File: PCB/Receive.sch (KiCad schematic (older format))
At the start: 40 parts

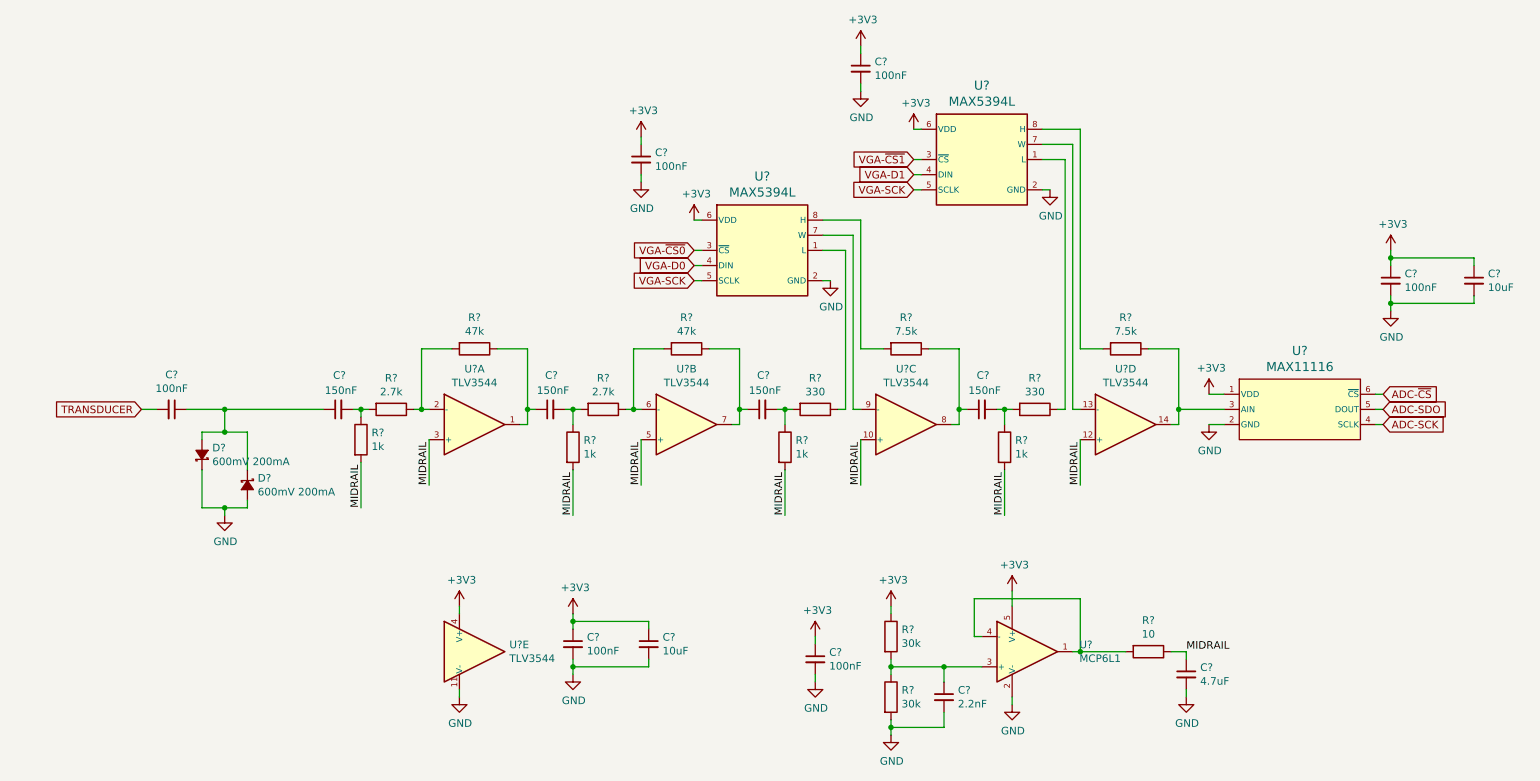
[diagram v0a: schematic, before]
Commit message: Switch 3.3V analog circuitry to low noise supply, fix pin classifications on some parts, swap 9V connector for 10V
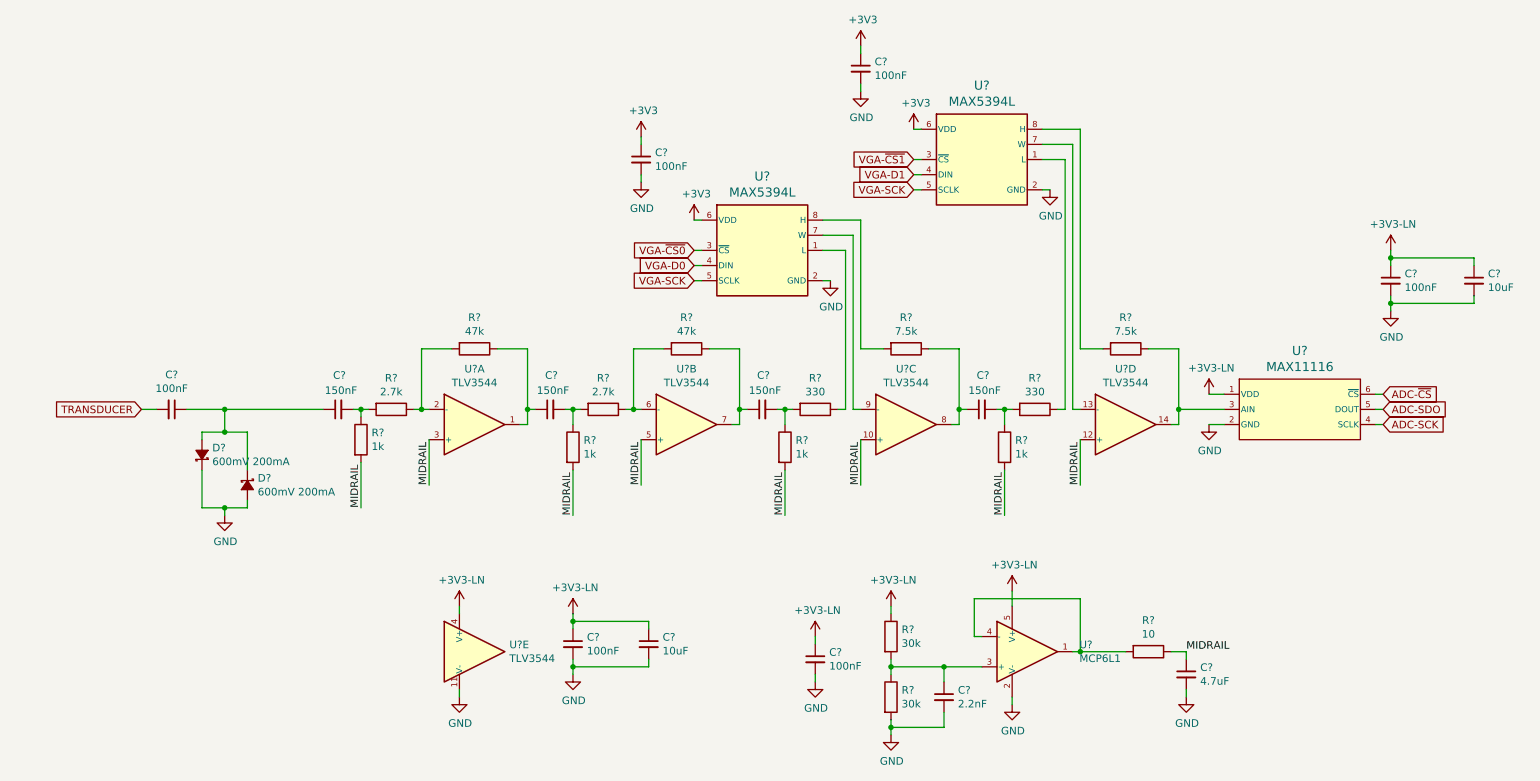
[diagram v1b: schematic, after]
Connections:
- net +3V3: no longer C?.1, C?.1, C?.1, C?.1, C?.1, R?.1, U?.1 (VDD), U?.4 (V+), U?.5 (V+)
- new net +3V3-LN: C?.1, C?.1, C?.1, C?.1, C?.1, R?.1, U?.1 (VDD), U?.4 (V+), U?.5 (V+)
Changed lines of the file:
@@
-$EndComp
-$Comp
-L power:+3V3 #PWR?
-U 1 1 5DE6A184
-P 8650 3650
-F 0 "#PWR?" H 8650 3500 50  0001 C CNN
-F 1 "+3V3" H 8665 3823 50  0000 C CNN
-F 2 "" H 8650 3650 50  0001 C CNN
-F 3 "" H 8650 3650 50  0001 C CNN
-	1    8650 3650
-	1    0    0    -1
 $EndComp
 $Comp
@@
 $EndComp
 $Comp
-L power:+3V3 #PWR?
-U 1 1 5E3D46BE
-P 9850 2700
-F 0 "#PWR?" H 9850 2550 50  0001 C CNN
-F 1 "+3V3" H 9865 2873 50  0000 C CNN
-F 2 "" H 9850 2700 50  0001 C CNN
-F 3 "" H 9850 2700 50  0001 C CNN
-	1    9850 2700
-	1    0    0    -1
-$EndComp
-$Comp
 L power:GND #PWR?
 U 1 1 5E3D4BAC
@@
 	2150 3750 2800 3750
 $Comp
-L power:+3V3 #PWR?
-U 1 1 5DF4FCE8
-P 6050 5250
-F 0 "#PWR?" H 6050 5100 50  0001 C CNN
-F 1 "+3V3" H 6065 5423 50  0000 C CNN
-F 2 "" H 6050 5250 50  0001 C CNN
-F 3 "" H 6050 5250 50  0001 C CNN
-	1    6050 5250
-	1    0    0    -1
-$EndComp
-$Comp
 L power:GND #PWR?
 U 1 1 5DF502DD
@@
 Wire Wire Line
 	4450 5450 4450 5500
-$Comp
-L power:+3V3 #PWR?
-U 1 1 5DF52ADC
-P 4450 5100
-F 0 "#PWR?" H 4450 4950 50  0001 C CNN
-F 1 "+3V3" H 4465 5273 50  0000 C CNN
-F 2 "" H 4450 5100 50  0001 C CNN
-F 3 "" H 4450 5100 50  0001 C CNN
-	1    4450 5100
-	1    0    0    -1
-$EndComp
-$Comp
-L power:+3V3 #PWR?
-U 1 1 5DF58761
-P 3700 5050
-F 0 "#PWR?" H 3700 4900 50  0001 C CNN
-F 1 "+3V3" H 3715 5223 50  0000 C CNN
-F 2 "" H 3700 5050 50  0001 C CNN
-F 3 "" H 3700 5050 50  0001 C CNN
-	1    3700 5050
-	1    0    0    -1
-$EndComp
 $Comp
 L power:GND #PWR?
@@
 Wire Wire Line
 	6100 2900 6150 2900
-$Comp
-L power:+3V3 #PWR?
-U 1 1 5DFD98EC
-P 5250 2500
-F 0 "#PWR?" H 5250 2350 50  0001 C CNN
-F 1 "+3V3" H 5265 2673 50  0000 C CNN
-F 2 "" H 5250 2500 50  0001 C CNN
-F 3 "" H 5250 2500 50  0001 C CNN
-	1    5250 2500
-	1    0    0    -1
-$EndComp
 Wire Wire Line
 	5250 2500 5300 2500
@@
 Wire Wire Line
 	7550 2300 7600 2300
-$Comp
-L power:+3V3 #PWR?
-U 1 1 5E033FD3
-P 6700 1900
-F 0 "#PWR?" H 6700 1750 50  0001 C CNN
-F 1 "+3V3" H 6715 2073 50  0000 C CNN
-F 2 "" H 6700 1900 50  0001 C CNN
-F 3 "" H 6700 1900 50  0001 C CNN
-	1    6700 1900
-	1    0    0    -1
-$EndComp
 Wire Wire Line
 	6700 1900 6750 1900
-$Comp
-L power:+3V3 #PWR?
-U 1 1 5E052B0A
-P 7350 4950
-F 0 "#PWR?" H 7350 4800 50  0001 C CNN
-F 1 "+3V3" H 7365 5123 50  0000 C CNN
-F 2 "" H 7350 4950 50  0001 C CNN
-F 3 "" H 7350 4950 50  0001 C CNN
-	1    7350 4950
-	1    0    0    -1
-$EndComp
 Wire Wire Line
 	7350 4950 7350 5050
@@
 Wire Wire Line
 	7300 4450 7300 4150
-$Comp
-L power:+3V3 #PWR?
-U 1 1 5E0A28B9
-P 6550 5050
-F 0 "#PWR?" H 6550 4900 50  0001 C CNN
-F 1 "+3V3" H 6565 5223 50  0000 C CNN
-F 2 "" H 6550 5050 50  0001 C CNN
-F 3 "" H 6550 5050 50  0001 C CNN
-	1    6550 5050
-	1    0    0    -1
-$EndComp
 $Comp
 L Device:R R?
@@
 	6350 2500 6350 3350
 $Comp
-L power:+3V3 #PWR?
-U 1 1 5E150771
-P 4900 1950
-F 0 "#PWR?" H 4900 1800 50  0001 C CNN
-F 1 "+3V3" H 4915 2123 50  0000 C CNN
-F 2 "" H 4900 1950 50  0001 C CNN
-F 3 "" H 4900 1950 50  0001 C CNN
-	1    4900 1950
-	1    0    0    -1
-$EndComp
-$Comp
 L power:GND #PWR?
 U 1 1 5E15077B
@@
 Wire Wire Line
 	4900 1950 4900 2000
-$Comp
-L power:+3V3 #PWR?
-U 1 1 5E168AD7
-P 6350 1350
-F 0 "#PWR?" H 6350 1200 50  0001 C CNN
-F 1 "+3V3" H 6365 1523 50  0000 C CNN
-F 2 "" H 6350 1350 50  0001 C CNN
-F 3 "" H 6350 1350 50  0001 C CNN
-	1    6350 1350
-	1    0    0    -1
-$EndComp
 $Comp
 L power:GND #PWR?
@@
 Wire Wire Line
 	5250 2900 5300 2900
+$Comp
+L power:+3V3 #PWR?
+U 1 1 5E033FD3
+P 6700 1900
+F 0 "#PWR?" H 6700 1750 50  0001 C CNN
+F 1 "+3V3" H 6715 2073 50  0000 C CNN
+F 2 "" H 6700 1900 50  0001 C CNN
+F 3 "" H 6700 1900 50  0001 C CNN
+	1    6700 1900
+	1    0    0    -1
+$EndComp
+$Comp
+L power:+3V3 #PWR?
+U 1 1 5E168AD7
+P 6350 1350
+F 0 "#PWR?" H 6350 1200 50  0001 C CNN
+F 1 "+3V3" H 6365 1523 50  0000 C CNN
+F 2 "" H 6350 1350 50  0001 C CNN
+F 3 "" H 6350 1350 50  0001 C CNN
+	1    6350 1350
+	1    0    0    -1
+$EndComp
+$Comp
+L power:+3V3 #PWR?
+U 1 1 5DFD98EC
+P 5250 2500
+F 0 "#PWR?" H 5250 2350 50  0001 C CNN
+F 1 "+3V3" H 5265 2673 50  0000 C CNN
+F 2 "" H 5250 2500 50  0001 C CNN
+F 3 "" H 5250 2500 50  0001 C CNN
+	1    5250 2500
+	1    0    0    -1
+$EndComp
+$Comp
+L power:+3V3 #PWR?
+U 1 1 5E150771
+P 4900 1950
+F 0 "#PWR?" H 4900 1800 50  0001 C CNN
+F 1 "+3V3" H 4915 2123 50  0000 C CNN
+F 2 "" H 4900 1950 50  0001 C CNN
+F 3 "" H 4900 1950 50  0001 C CNN
+	1    4900 1950
+	1    0    0    -1
+$EndComp
+$Comp
+L Parts:+3V3-LN #PWR?
+U 1 1 5E2A82B0
+P 8650 3650
+F 0 "#PWR?" H 8650 3500 50  0001 C CNN
+F 1 "+3V3-LN" H 8665 3823 50  0000 C CNN
+F 2 "" H 8650 3650 50  0001 C CNN
+F 3 "" H 8650 3650 50  0001 C CNN
+	1    8650 3650
+	1    0    0    -1
+$EndComp
+$Comp
+L Parts:+3V3-LN #PWR?
+U 1 1 5E2AAEEA
+P 6550 5050
+F 0 "#PWR?" H 6550 4900 50  0001 C CNN
+F 1 "+3V3-LN" H 6565 5223 50  0000 C CNN
+F 2 "" H 6550 5050 50  0001 C CNN
+F 3 "" H 6550 5050 50  0001 C CNN
+	1    6550 5050
+	1    0    0    -1
+$EndComp
+$Comp
+L Parts:+3V3-LN #PWR?
+U 1 1 5E2AD2A7
+P 9850 2700
+F 0 "#PWR?" H 9850 2550 50  0001 C CNN
+F 1 "+3V3-LN" H 9865 2873 50  0000 C CNN
+F 2 "" H 9850 2700 50  0001 C CNN
+F 3 "" H 9850 2700 50  0001 C CNN
+	1    9850 2700
+	1    0    0    -1
+$EndComp
+$Comp
+L Parts:+3V3-LN #PWR?
+U 1 1 5E2AFA32
+P 7350 4950
+F 0 "#PWR?" H 7350 4800 50  0001 C CNN
+F 1 "+3V3-LN" H 7365 5123 50  0000 C CNN
+F 2 "" H 7350 4950 50  0001 C CNN
+F 3 "" H 7350 4950 50  0001 C CNN
+	1    7350 4950
+	1    0    0    -1
+$EndComp
+$Comp
+L Parts:+3V3-LN #PWR?
+U 1 1 5E2AFFB8
+P 6050 5250
+F 0 "#PWR?" H 6050 5100 50  0001 C CNN
+F 1 "+3V3-LN" H 6065 5423 50  0000 C CNN
+F 2 "" H 6050 5250 50  0001 C CNN
+F 3 "" H 6050 5250 50  0001 C CNN
+	1    6050 5250
+	1    0    0    -1
+$EndComp
+$Comp
+L Parts:+3V3-LN #PWR?
+U 1 1 5E2B0647
+P 4450 5100
+F 0 "#PWR?" H 4450 4950 50  0001 C CNN
+F 1 "+3V3-LN" H 4465 5273 50  0000 C CNN
+F 2 "" H 4450 5100 50  0001 C CNN
+F 3 "" H 4450 5100 50  0001 C CNN
+	1    4450 5100
+	1    0    0    -1
+$EndComp
+$Comp
+L Parts:+3V3-LN #PWR?
+U 1 1 5E2B0FA3
+P 3700 5050
+F 0 "#PWR?" H 3700 4900 50  0001 C CNN
+F 1 "+3V3-LN" H 3715 5223 50  0000 C CNN
+F 2 "" H 3700 5050 50  0001 C CNN
+F 3 "" H 3700 5050 50  0001 C CNN
+	1    3700 5050
+	1    0    0    -1
+$EndComp
 $EndSCHEMATC

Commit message: Annotate schematic, simplify transmit circuit, shuffle receive opamp stages, reorder buttons so they match net names, reorder connectors to simplify routing, begin arranging parts on PCB
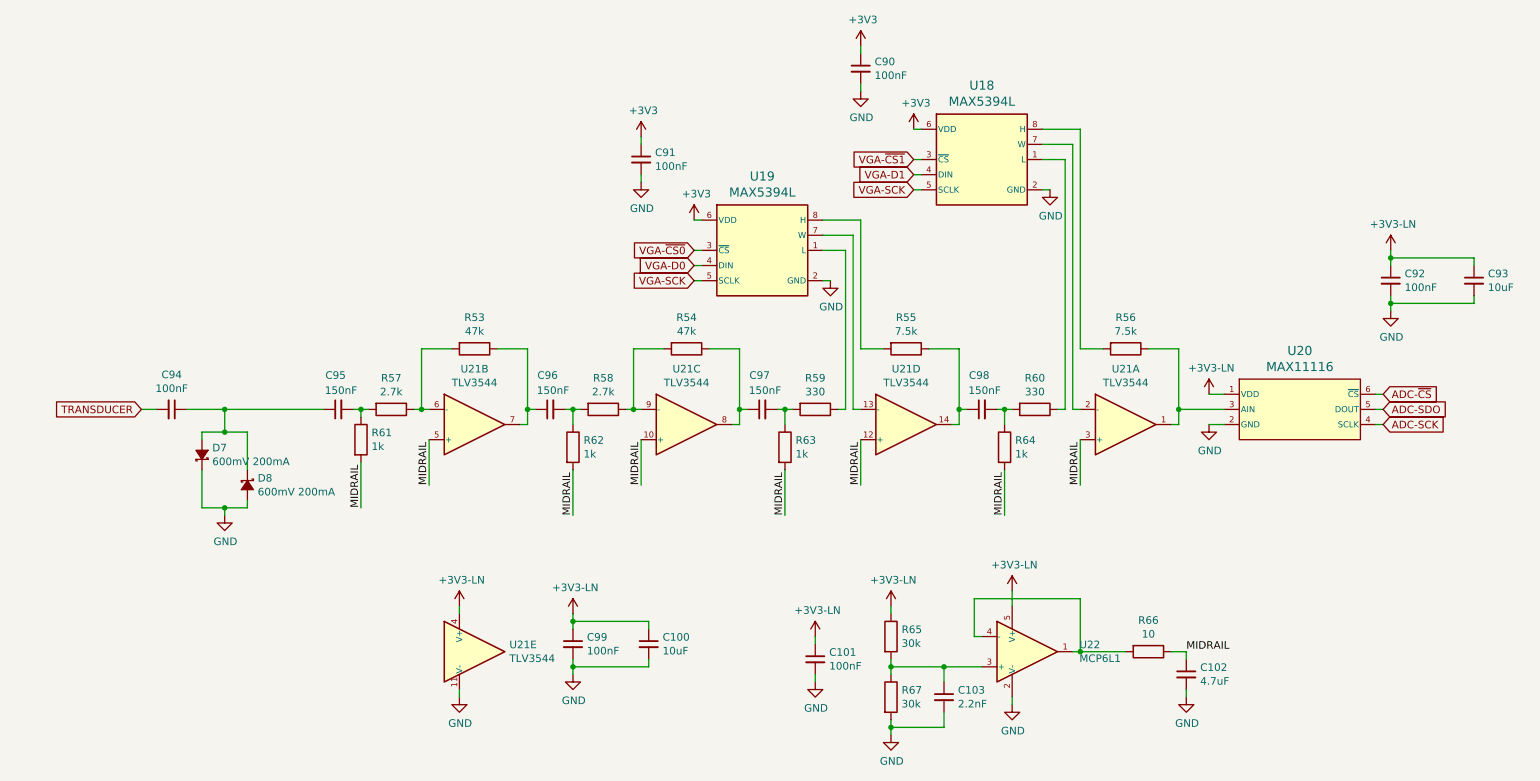
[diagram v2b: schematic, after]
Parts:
- gave numbers to parts that had none: 36
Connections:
- net at R56.1, U20.3 (AIN): now also U21.1; no longer U21.14
- net at C96.1, R53.1: now also U21.7; no longer U21.1
- net at R53.2, R57.1: now also U21.6 (-); no longer U21.2 (-)
- net at R54.2, R58.1: now also U21.9 (-); no longer U21.6 (-)
- net at C97.1, R54.1: now also U21.8; no longer U21.7
- net at C98.1, R55.1: now also U21.14; no longer U21.8
- net at U19.7 (W): now also U21.13 (-); no longer U21.9 (-)
- net at U18.7 (W): now also U21.2 (-); no longer U21.13 (-)
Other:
- moved on the sheet: U21A, U21B, U21C, U21D

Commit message: Begin layout around FPGA and microcontroller, rearrange some connections to FPGA and microcontroller, change groupings of optional debug pins
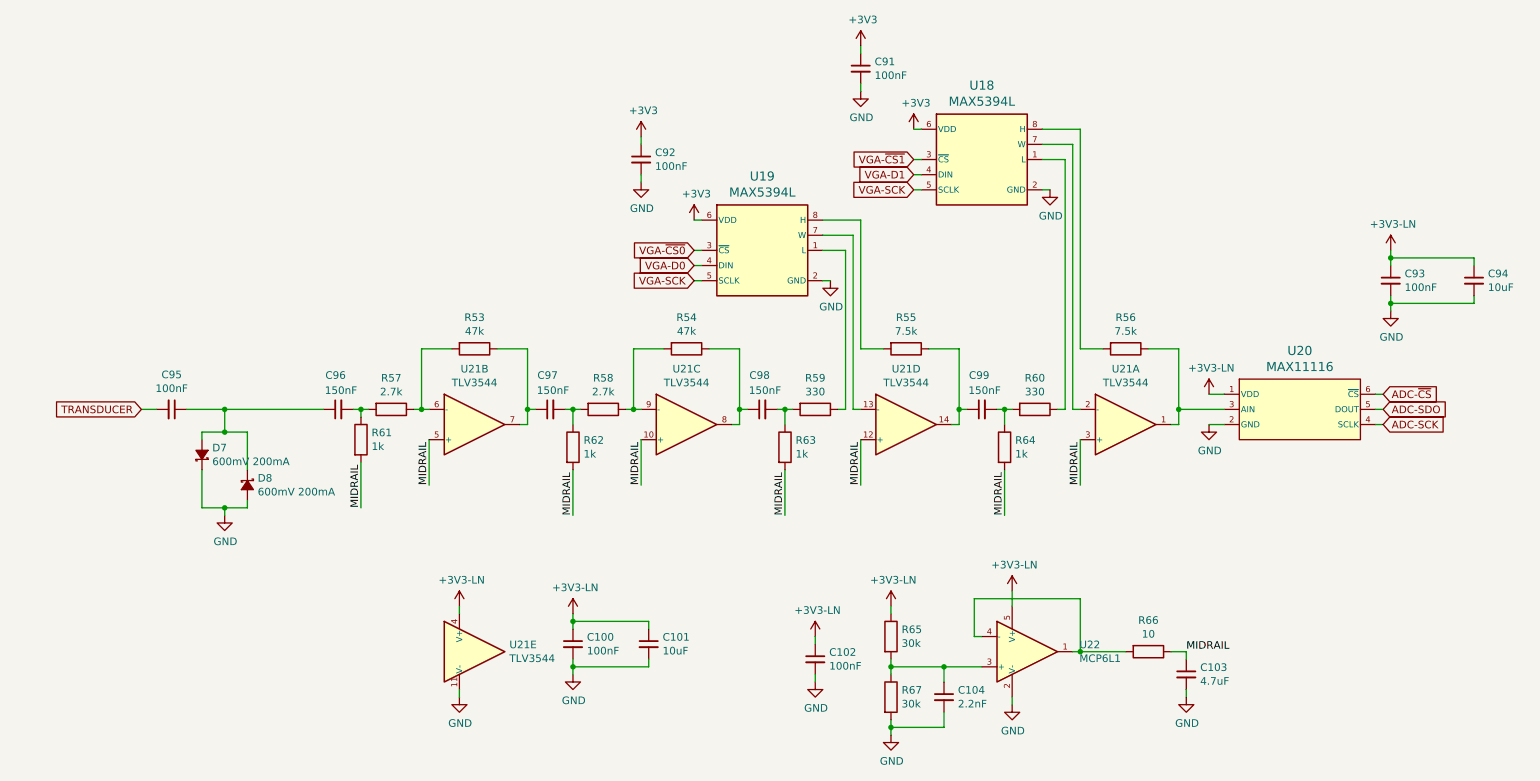
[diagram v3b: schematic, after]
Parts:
- renumbered C99 to C100, C100 to C101, C101 to C102, C102 to C103, C103 to C104, C90 to C91, C91 to C92, C92 to C93, C93 to C94, C94 to C95, C95 to C96, C96 to C97, C97 to C98, C98 to C99
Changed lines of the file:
@@
 $EndComp
 $Comp
-L Device:C_Small C94
+L Device:C_Small C95
 U 1 1 5DE7BD62
 P 1800 3750
-F 0 "C94" V 1571 3750 50  0000 C CNN
+F 0 "C95" V 1571 3750 50  0000 C CNN
 F 1 "100nF" V 1662 3750 50  0000 C CNN
 F 2 "Capacitors_SMD:C_1206_HandSoldering" H 1800 3750 50  0001 C CNN
@@
 	2150 4400 2300 4400
 $Comp
-L Device:C_Small C93
+L Device:C_Small C94
 U 1 1 5E3D409D
 P 10400 2900
-F 0 "C93" H 10492 2946 50  0000 L CNN
+F 0 "C94" H 10492 2946 50  0000 L CNN
 F 1 "10uF" H 10492 2855 50  0000 L CNN
 F 2 "Capacitors_SMD:C_0805_HandSoldering" H 10400 2900 50  0001 C CNN
@@
 $EndComp
 $Comp
-L Device:C_Small C92
+L Device:C_Small C93
 U 1 1 5E3D52F8
 P 9850 2900
-F 0 "C92" H 9942 2946 50  0000 L CNN
+F 0 "C93" H 9942 2946 50  0000 L CNN
 F 1 "100nF" H 9942 2855 50  0000 L CNN
 F 2 "Capacitors_SMD:C_0603_HandSoldering" H 9850 2900 50  0001 C CNN
@@
 Connection ~ 9850 3050
 $Comp
-L Device:C_Small C99
+L Device:C_Small C100
 U 1 1 5E132FDE
 P 4450 5300
-F 0 "C99" H 4542 5346 50  0000 L CNN
+F 0 "C100" H 4542 5346 50  0000 L CNN
 F 1 "100nF" H 4542 5255 50  0000 L CNN
 F 2 "Capacitors_SMD:C_0603_HandSoldering" H 4450 5300 50  0001 C CNN
@@
 $EndComp
 $Comp
-L Device:C_Small C101
+L Device:C_Small C102
 U 1 1 5E133797
 P 6050 5400
-F 0 "C101" H 6142 5446 50  0000 L CNN
+F 0 "C102" H 6142 5446 50  0000 L CNN
 F 1 "100nF" H 6142 5355 50  0000 L CNN
 F 2 "Capacitors_SMD:C_0603_HandSoldering" H 6050 5400 50  0001 C CNN
@@
 $EndComp
 $Comp
-L Device:C_Small C100
+L Device:C_Small C101
 U 1 1 5E133C95
 P 4950 5300
-F 0 "C100" H 5042 5346 50  0000 L CNN
+F 0 "C101" H 5042 5346 50  0000 L CNN
 F 1 "10uF" H 5042 5255 50  0000 L CNN
 F 2 "Capacitors_SMD:C_0805_HandSoldering" H 4950 5300 50  0001 C CNN
@@
 	3700 5050 3700 5100
 $Comp
-L Device:C_Small C95
+L Device:C_Small C96
 U 1 1 5DF5C548
 P 2900 3750
-F 0 "C95" V 3125 3700 50  0000 L CNN
+F 0 "C96" V 3125 3700 50  0000 L CNN
 F 1 "150nF" V 3025 3625 50  0000 L CNN
 F 2 "Capacitors_SMD:C_0603_HandSoldering" H 2900 3750 50  0001 C CNN
@@
 	4150 3350 4150 3750
 $Comp
-L Device:C_Small C96
+L Device:C_Small C97
 U 1 1 5DF78526
 P 4300 3750
-F 0 "C96" V 4525 3700 50  0000 L CNN
+F 0 "C97" V 4525 3700 50  0000 L CNN
 F 1 "150nF" V 4425 3625 50  0000 L CNN
 F 2 "Capacitors_SMD:C_0603_HandSoldering" H 4300 3750 50  0001 C CNN
@@
 	5550 3750 5550 3850
 $Comp
-L Device:C_Small C97
+L Device:C_Small C98
 U 1 1 5DF8BDC4
 P 5700 3750
-F 0 "C97" V 5925 3700 50  0000 L CNN
+F 0 "C98" V 5925 3700 50  0000 L CNN
 F 1 "150nF" V 5825 3625 50  0000 L CNN
 F 2 "Capacitors_SMD:C_0603_HandSoldering" H 5700 3750 50  0001 C CNN
@@
 	6250 3750 6200 3750
 $Comp
-L Device:C_Small C98
+L Device:C_Small C99
 U 1 1 5DFF8C03
 P 7150 3750
-F 0 "C98" V 7375 3700 50  0000 L CNN
+F 0 "C99" V 7375 3700 50  0000 L CNN
 F 1 "150nF" V 7275 3625 50  0000 L CNN
 F 2 "Capacitors_SMD:C_0603_HandSoldering" H 7150 3750 50  0001 C CNN
@@
 $EndComp
 $Comp
-L Device:C_Small C103
+L Device:C_Small C104
 U 1 1 5E0D9D1C
 P 6900 5650
-F 0 "C103" H 6992 5696 50  0000 L CNN
+F 0 "C104" H 6992 5696 50  0000 L CNN
 F 1 "2.2nF" H 6992 5605 50  0000 L CNN
 F 2 "Capacitors_SMD:C_0603_HandSoldering" H 6900 5650 50  0001 C CNN
@@
 	6550 5850 6550 5900
 $Comp
-L Device:C_Small C102
+L Device:C_Small C103
 U 1 1 5E0E564B
 P 8500 5500
-F 0 "C102" H 8592 5546 50  0000 L CNN
+F 0 "C103" H 8592 5546 50  0000 L CNN
 F 1 "4.7uF" H 8592 5455 50  0000 L CNN
 F 2 "Capacitors_SMD:C_0603_HandSoldering" H 8500 5500 50  0001 C CNN
@@
 $EndComp
 $Comp
-L Device:C_Small C91
+L Device:C_Small C92
 U 1 1 5E150785
 P 4900 2100
-F 0 "C91" H 4992 2146 50  0000 L CNN
+F 0 "C92" H 4992 2146 50  0000 L CNN
 F 1 "100nF" H 4992 2055 50  0000 L CNN
 F 2 "Capacitors_SMD:C_0603_HandSoldering" H 4900 2100 50  0001 C CNN
@@
 $EndComp
 $Comp
-L Device:C_Small C90
+L Device:C_Small C91
 U 1 1 5E168AEB
 P 6350 1500
-F 0 "C90" H 6442 1546 50  0000 L CNN
+F 0 "C91" H 6442 1546 50  0000 L CNN
 F 1 "100nF" H 6442 1455 50  0000 L CNN
 F 2 "Capacitors_SMD:C_0603_HandSoldering" H 6350 1500 50  0001 C CNN
